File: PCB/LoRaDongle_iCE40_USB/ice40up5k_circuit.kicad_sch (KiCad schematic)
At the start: 28 parts, among them IC2 ICE40UP5K-UWG30ITR1K, IC3 N25Q032A13ESC40F, J10 Jumper_2_Open, J3 Conn_02x02_Top_Bottom, J6 Conn_01x06, J7 Jumper_NC_Small, J9 Conn_02x02_Top_Bottom, SW1 SW_Push, X1 ECS-2520MV-500-BL-TR

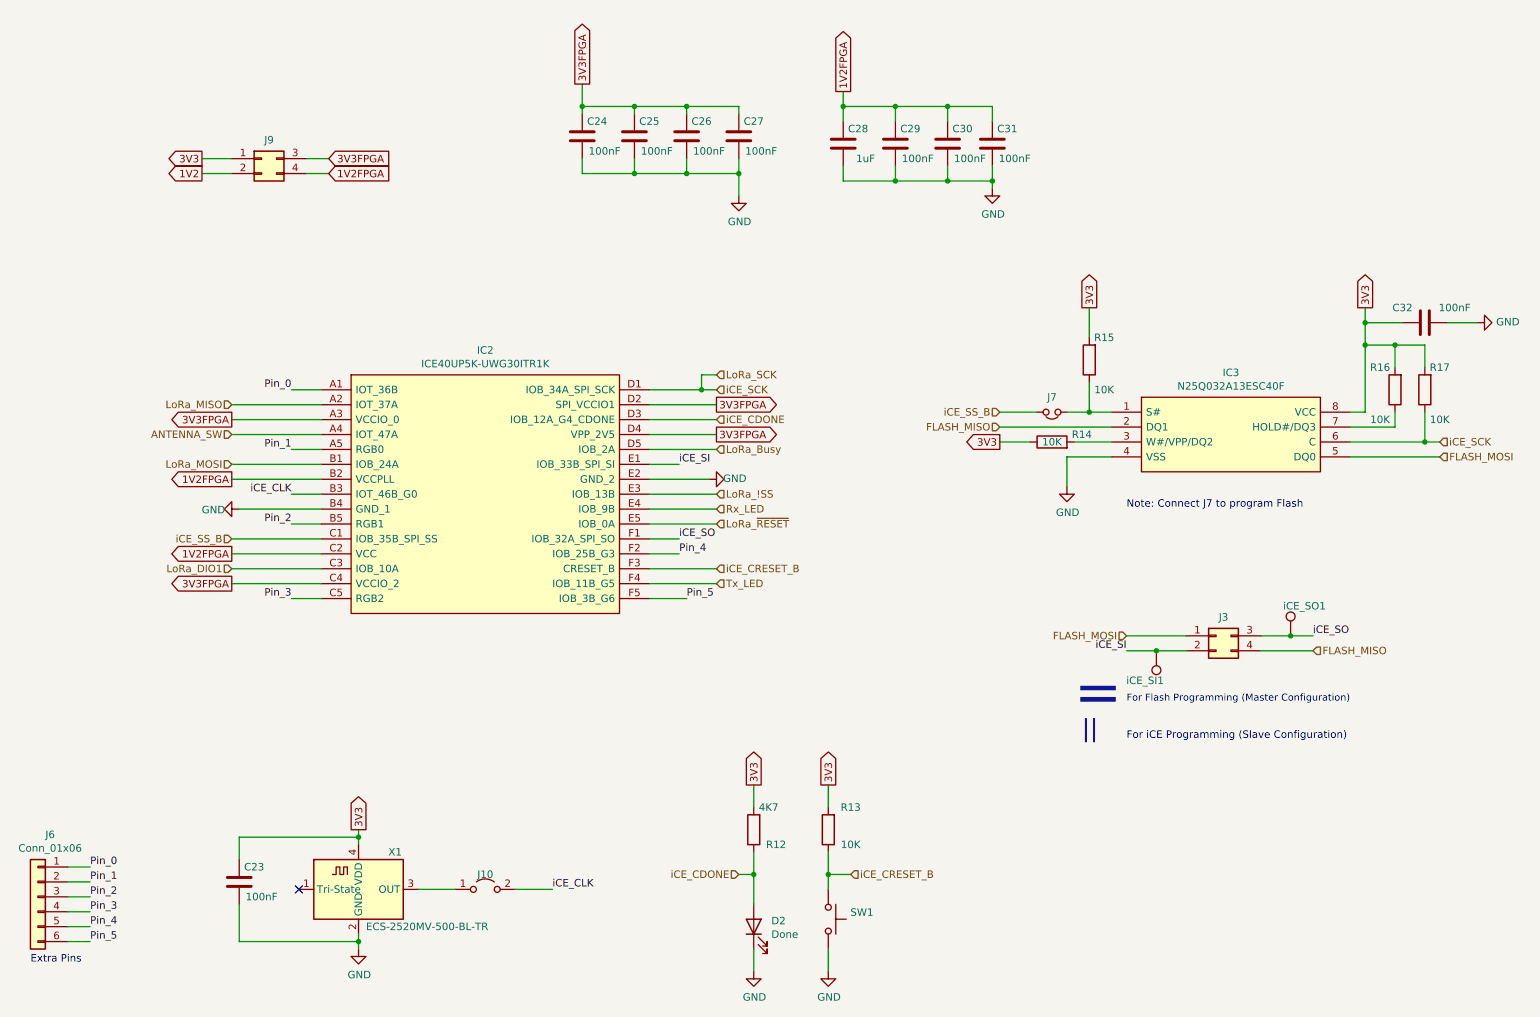
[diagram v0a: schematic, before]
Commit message: updated ftdi and flash chip, removed xilinx project
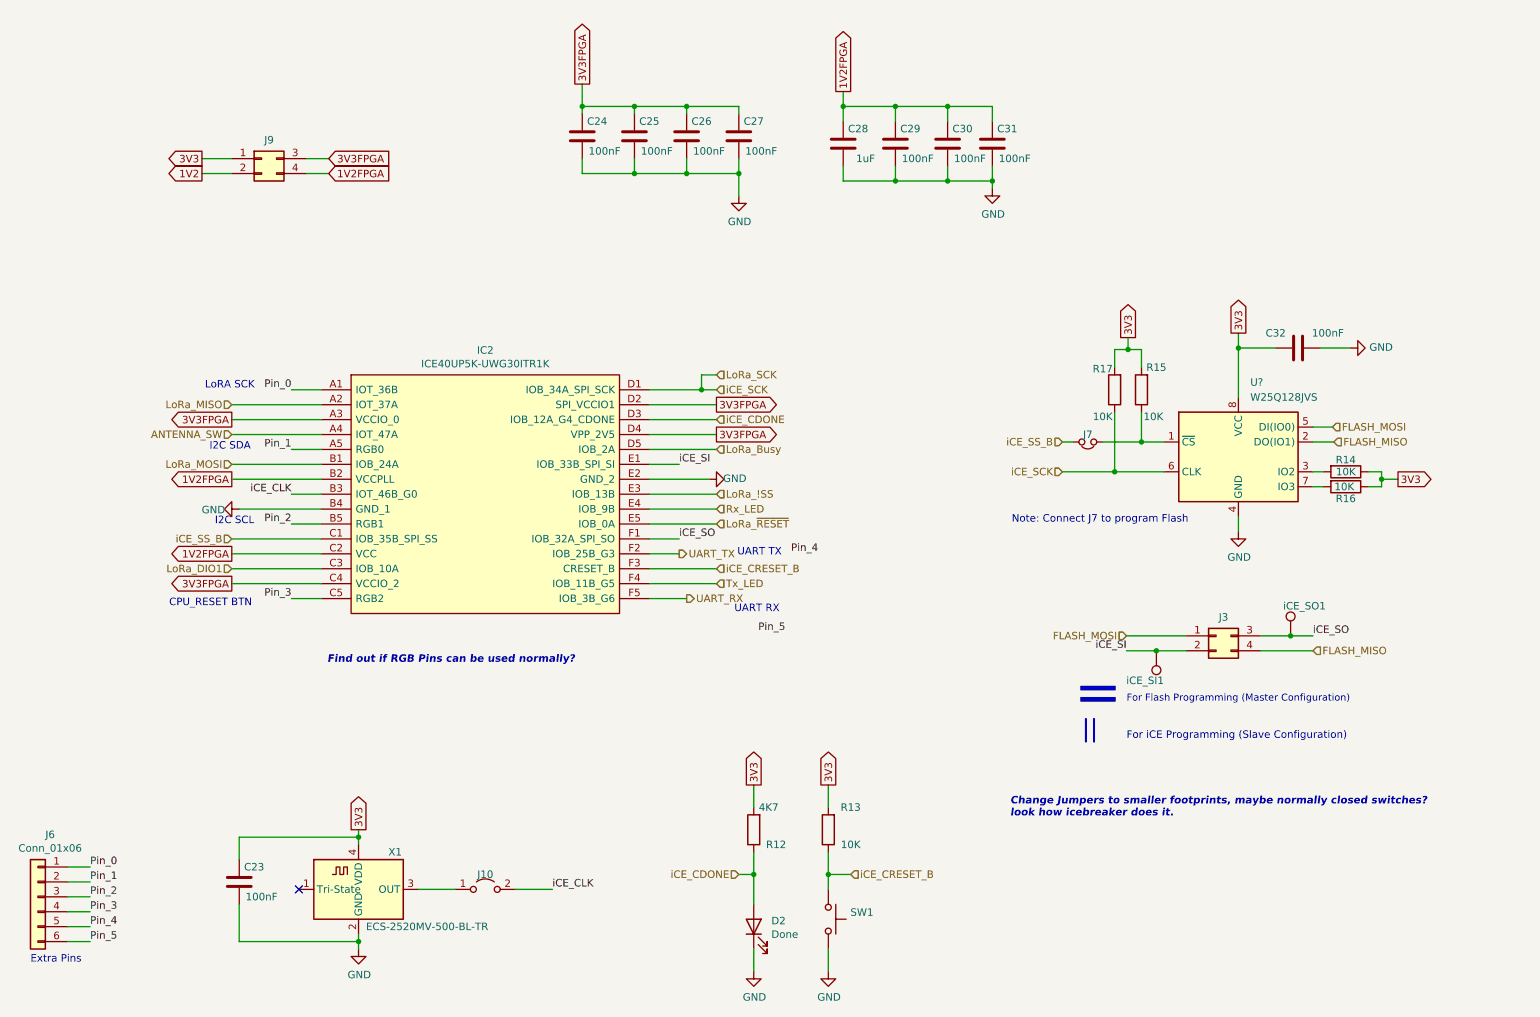
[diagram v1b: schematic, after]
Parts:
- removed IC3: N25Q032A13ESC40F, N25Q032A13ESC40F:SOIC127P600X175-8N, symbol N25Q032A13ESC40F:N25Q032A13ESC40F
- added U?: W25Q128JVS, Package_SO:SOIC-8_5.23x5.23mm_P1.27mm, symbol Memory_Flash:W25Q128JVS
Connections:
- net 3V3: now also R16.1, U?.8 (VCC); no longer R16.2
- net FLASH_MISO: now also U?.2 (DO(IO1))
- net FLASH_MOSI: now also U?.5 (DI(IO0))
- net GND: now also U?.4 (GND)
- net LoRa_SCK: now also U?.6 (CLK)
- net Pin_4: no longer IC2.F2 (IOB_25B_G3)
- net Pin_5: no longer IC2.F5 (IOB_3B_G6)
- net at J7.1, R15.1: now also U?.1 (~{CS})
- net at R14.2: now also U?.3 (IO2)
- new net: R16.2, U?.7 (IO3)
- new net UART_RX: IC2.F5 (IOB_3B_G6)
- new net UART_TX: IC2.F2 (IOB_25B_G3)
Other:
- note added: "CPU_RESET BTN"
- note added: "Change Jumpers to smaller footprints, maybe normally closed switches? look how icebreaker does it."
- note added: "Find out if RGB Pins can be used normally?"
- note added: "I2C SCL"
- note added: "I2C SDA"
- note added: "LoRA SCK"
- note added: "UART RX"
- note added: "UART TX"
- moved on the sheet: C32, J7, R14, R15, R16, R17

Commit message: updated jumpers, connectors and testpoints
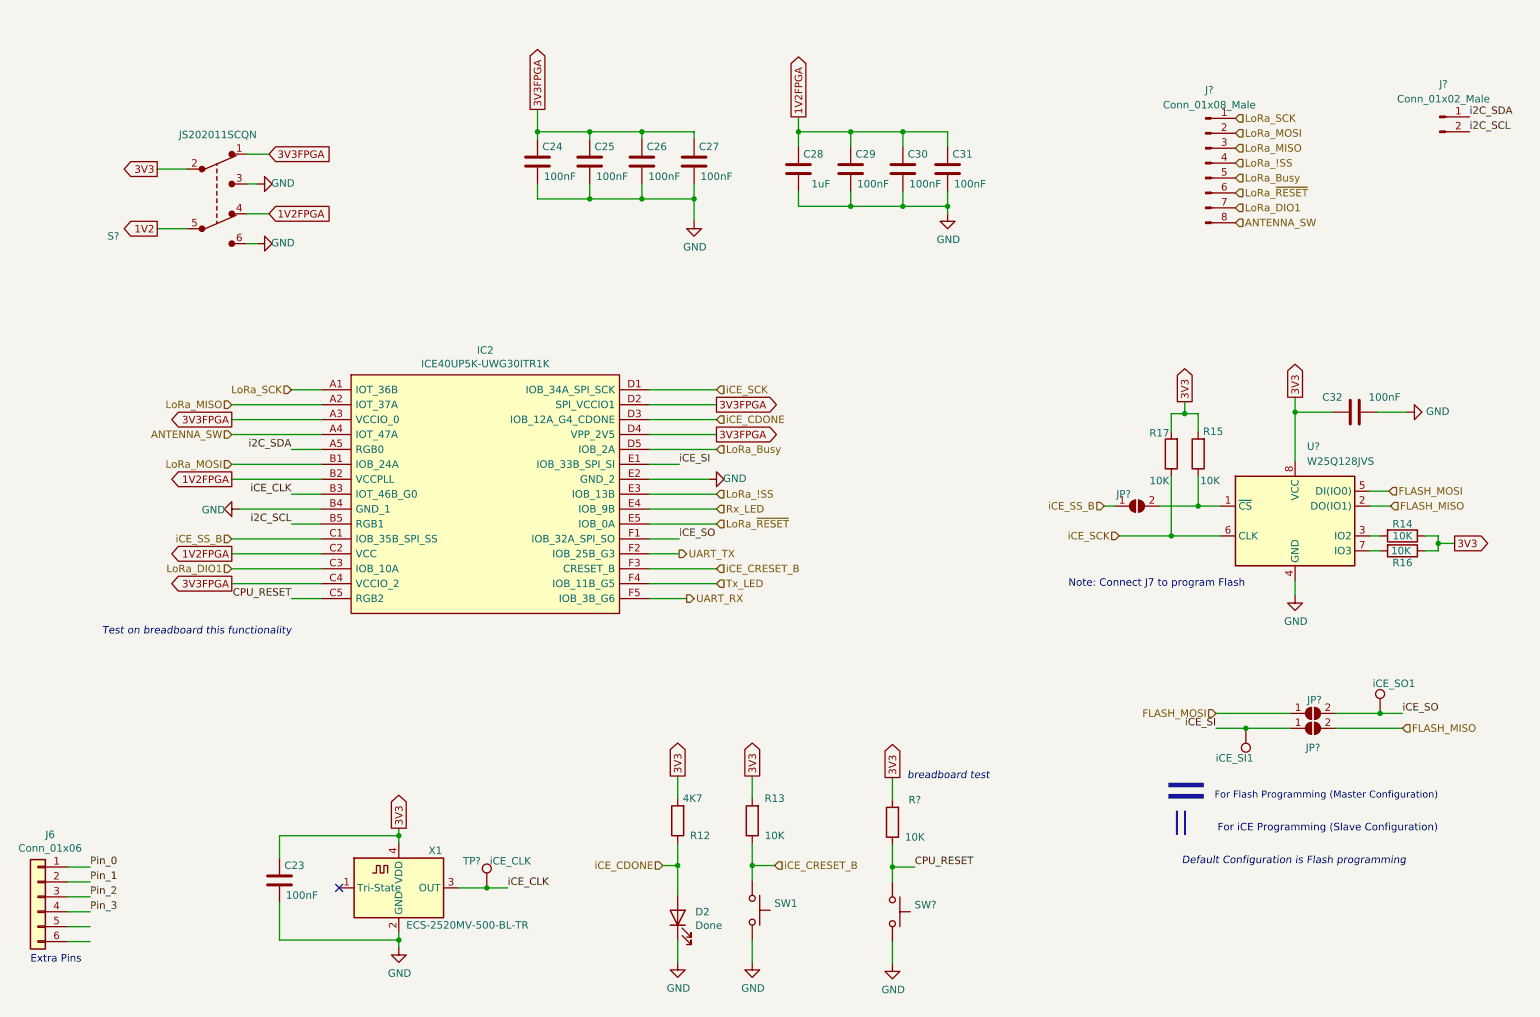
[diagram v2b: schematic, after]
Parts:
- removed J10: Jumper_2_Open, Connector_PinHeader_2.54mm:PinHeader_1x02_P2.54mm_Vertical, symbol Jumper:Jumper_2_Open
- removed J3, J9: Conn_02x02_Top_Bottom, Connector_PinHeader_2.54mm:PinHeader_2x02_P2.54mm_Vertical, symbol Connector_Generic:Conn_02x02_Top_Bottom
- removed J7: Jumper_NC_Small, Connector_PinHeader_2.54mm:PinHeader_1x02_P2.54mm_Vertical, symbol Device:Jumper_NC_Small
- added J?: Conn_01x02_Male, symbol Connector:Conn_01x02_Male
- added J?: Conn_01x08_Male, symbol Connector:Conn_01x08_Male
- added JP? (x3): SolderJumper_2_Open, Resistor_SMD:R_0603_1608Metric_Pad0.98x0.95mm_HandSolder, symbol Jumper:SolderJumper_2_Open
- added R?: 10K, Resistor_SMD:R_0402_1005Metric_Pad0.72x0.64mm_HandSolder, symbol Device:R
- added S?: JS202011SCQN, digikey-footprints:Switch_Slide_JS202011SCQN, symbol dk_Slide-Switches:JS202011SCQN
- added SW?: SW_Push, Button_Switch_THT:SW_PUSH_6mm_H5mm, symbol Switch:SW_Push
- added TP?: iCE_CLK, symbol Connector:TestPoint
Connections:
- net 1V2: now also S?.5
- net 1V2FPGA: now also S?.4
- net 3V3: now also R?.2, S?.2
- net 3V3FPGA: now also S?.1
- net ANTENNA_SW: now also J?.8 (Pin_8)
- net FLASH_MISO: now also JP?.2 (B)
- net FLASH_MOSI: now also JP?.1 (A)
- net GND: now also S?.3, S?.6, SW?.2
- net LoRa_!SS: now also J?.4 (Pin_4)
- net LoRa_Busy: now also J?.5 (Pin_5)
- net LoRa_DIO1: now also J?.7 (Pin_7)
- net LoRa_MISO: now also J?.3 (Pin_3)
- net LoRa_MOSI: now also J?.2 (Pin_2)
- net LoRa_SCK: now also IC2.A1 (IOT_36B), J?.1 (Pin_1); no longer IC2.D1 (IOB_34A_SPI_SCK), R17.1, U?.6 (CLK)
- net LoRa_~{RESET}: now also J?.6 (Pin_6)
- net Pin_0: no longer IC2.A1 (IOT_36B)
- net Pin_1: no longer IC2.A5 (RGB0)
- net Pin_2: no longer IC2.B5 (RGB1)
- net Pin_3: no longer IC2.C5 (RGB2)
- net iCE_CLK: now also X1.3 (OUT), TP?.1
- net iCE_SI: now also JP?.1 (A)
- net iCE_SO: now also JP?.2 (B)
- net iCE_SS_B: now also JP?.1 (A)
- net at R15.1, U?.1 (~{CS}): now also JP?.2 (B)
- net Pin_4: no longer names the net of J6.5 (Pin_5)
- net Pin_5: no longer names the net of J6.6 (Pin_6)
- new net CPU_RESET: IC2.C5 (RGB2), R?.1, SW?.1
- new net i2C_SCL: IC2.B5 (RGB1), J?.2 (Pin_2)
- new net i2C_SDA: IC2.A5 (RGB0), J?.1 (Pin_1)
- new net iCE_SCK: IC2.D1 (IOB_34A_SPI_SCK), R17.1, U?.6 (CLK)
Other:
- note added: "Default Configuration is Flash programming"
- note added: "Test on breadboard this functionality"
- note added: "breadboard test"
- note removed: "CPU_RESET BTN"
- note removed: "Change Jumpers to smaller footprints, maybe normally closed switches? look how icebreaker does it."
- note removed: "Find out if RGB Pins can be used normally?"
- note removed: "I2C SCL"
- note removed: "I2C SDA"
- note removed: "LoRA SCK"
- note removed: "UART RX"
- note removed: "UART TX"
- moved on the sheet: C23, C24, C25, C26, C27, C28, C29, C30, C31, C32, D2, R12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
